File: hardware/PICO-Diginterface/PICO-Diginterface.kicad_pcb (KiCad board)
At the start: 2 copper layers, 95 x 70 mm, 27 parts

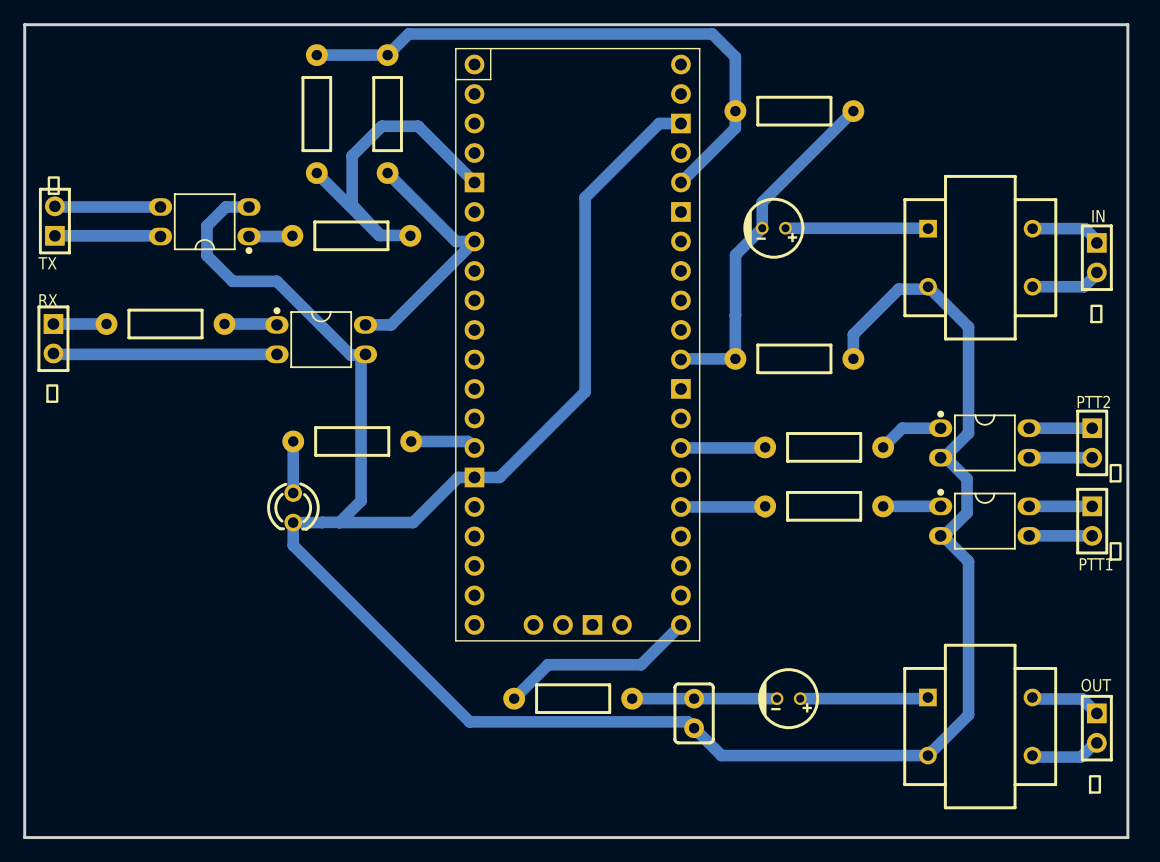
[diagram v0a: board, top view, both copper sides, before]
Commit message: hardware change: common grounds on radio side
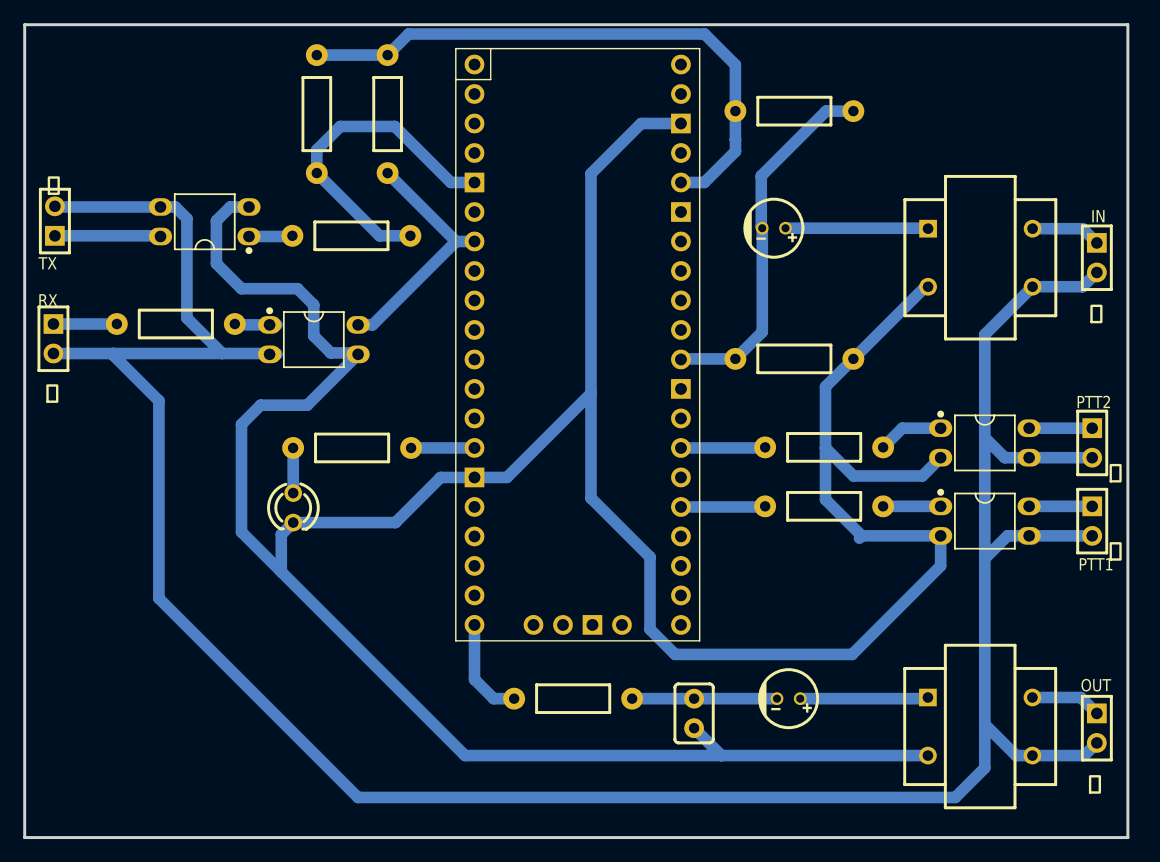
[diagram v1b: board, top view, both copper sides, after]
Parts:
- C1, C2: footprint PICO-Digin-easyedapro:CAP-TH_BD5.0-P2.00-D0.5-FD_CD26G2AM1R0D110T -> ProPrj_PIC-easyedapro:CAP-TH_BD5.0-P2.00-D0.5-FD_CD26G2AM1R0D110T
- C14: footprint PICO-Digin-easyedapro:CAP-TH_L5.1-W3.2-P2.54-D0.5 -> ProPrj_PIC-easyedapro:CAP-TH_L5.1-W3.2-P2.54-D0.5
- H1, H2, H3, H4, H5, H6: footprint PICO-Digin-easyedapro:HDR-TH_2P-P2.54-V-F -> ProPrj_PIC-easyedapro:HDR-TH_2P-P2.54-V-F
- LED1: footprint PICO-Digin-easyedapro:LED-TH_BD3.0-P2.54-FD -> ProPrj_PIC-easyedapro:LED-TH_BD3.0-P2.54-FD
- R10, R12, R13, R15, R16, R17, R18, R7, R8, R9: footprint PICO-Digin-easyedapro:R_AXIAL-0.4 -> ProPrj_PIC-easyedapro:R_AXIAL-0.4
- TR1, TR2: footprint PICO-Digin-easyedapro:1{colon}1 TRANSFORMER -> ProPrj_PIC-easyedapro:1{colon}1 TRANSFORMER
- U10, U11, U12, U9: footprint PICO-Digin-easyedapro:DIP-4_L4.6-W6.5-P2.54-LS7.6-BL -> ProPrj_PIC-easyedapro:DIP-4_L4.6-W6.5-P2.54-LS7.6-BL
- U5: footprint PICO-Digin-easyedapro:PurplePICORP2040TH -> ProPrj_PIC-easyedapro:PurplePICORP2040TH
- moved R7 0.89 mm to (113.0, 95.8)
- moved U10 0.63 mm to (124.9, 97.1)
- moved R15 0.56 mm to (128.2, 106.4)
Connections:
- H1 pad 2: $1N1689 -> RADIOGND
- H2 pad 2: $1N4713 -> RADIOGND
- H3 pad 2: $1N2393 -> RADIOGND
- H4 pad 2: $1N4831 -> RADIOGND
- H5 pad 2: $1N5404 -> RADIOGND
- H6 pad 2: $1N3831 -> RADIOGND
- R9 pad 1: $1N5539 -> $1N5543
- TR1 pad 4: $1N5404 -> RADIOGND
- TR2 pad 4: $1N3831 -> RADIOGND
- U10 pad 2: $1N1689 -> RADIOGND
- U11 pad 3: $1N2393 -> RADIOGND
- U12 pad 3: $1N4831 -> RADIOGND
- U5 pad 20: (no net) -> $1N5543
- U5 pad 21: $1N5539 -> (no net)
- U9 pad 3: $1N4713 -> RADIOGND
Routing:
- net RADIOGND: track 0.00 -> 226.4 mm
- net GND: track 218.4 -> 278.9 mm
- net $1N1689: track 19.3 -> 0.00 mm
- net $1N5539: track 17.0 -> 0.00 mm
- net $1N4713: track 9.12 -> 0.00 mm
- net $1N5543: track 0.00 -> 8.80 mm
- net $1N5404: track 6.39 -> 0.00 mm
- net $1N3831: track 5.99 -> 0.00 mm
- net $1N4831: track 5.43 -> 0.00 mm
- net $1N2393: track 5.43 -> 0.00 mm
- net $1N4725: track 31.7 -> 28.7 mm
- net $1N1419: track 22.3 -> 20.7 mm
- net $1N2953: track 30.3 -> 31.7 mm
- net $1N1678: track 4.57 -> 5.59 mm
- net $1N291: track 4.55 -> 3.53 mm
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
